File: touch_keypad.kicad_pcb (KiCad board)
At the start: 2 copper layers, 64.8 x 81.3 mm, 43 parts, among them J1 USB_B_Micro, J5 Conn_01x04_Female, SW1 SW_Push, SW10 SW_Push, SW11 SW_Push, SW12 SW_Push, SW13 SW_Push, SW14 SW_Push, SW15 SW_Push, SW16 SW_Push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

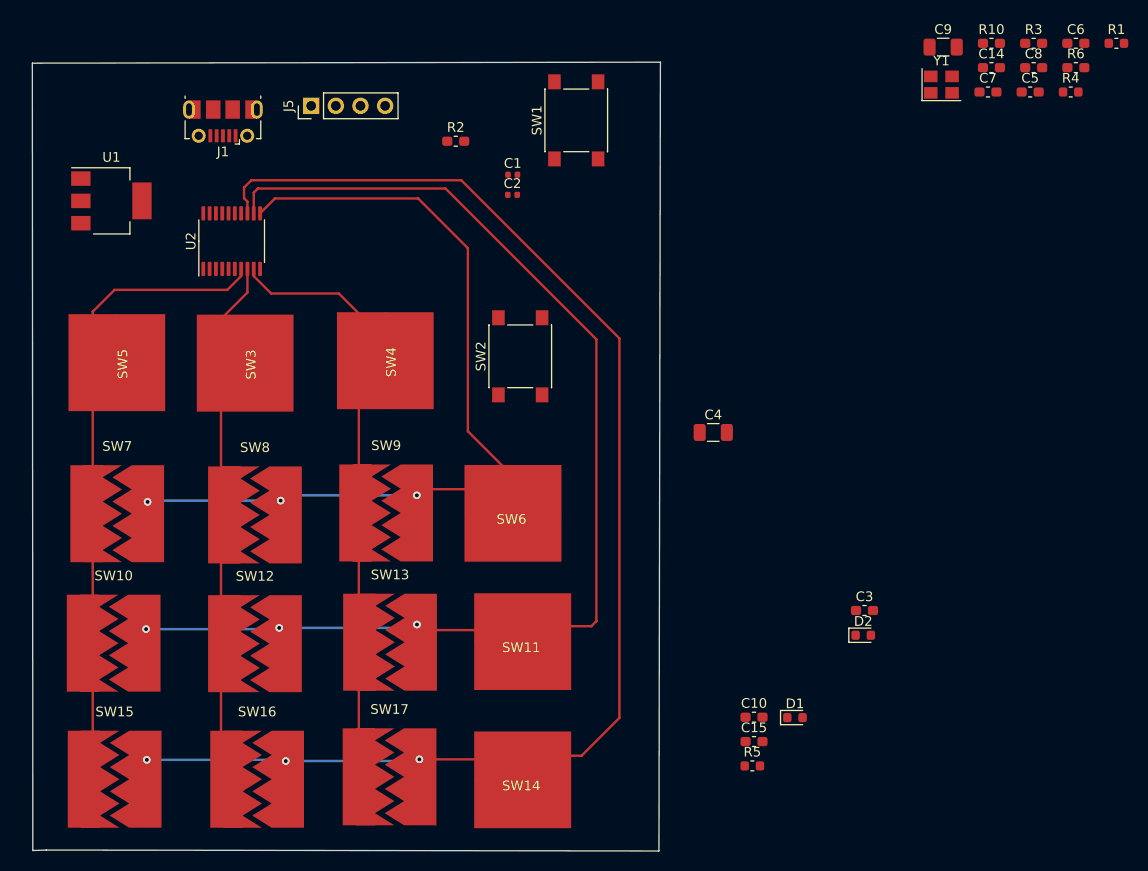
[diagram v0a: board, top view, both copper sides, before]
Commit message: upgrade to kicad 6
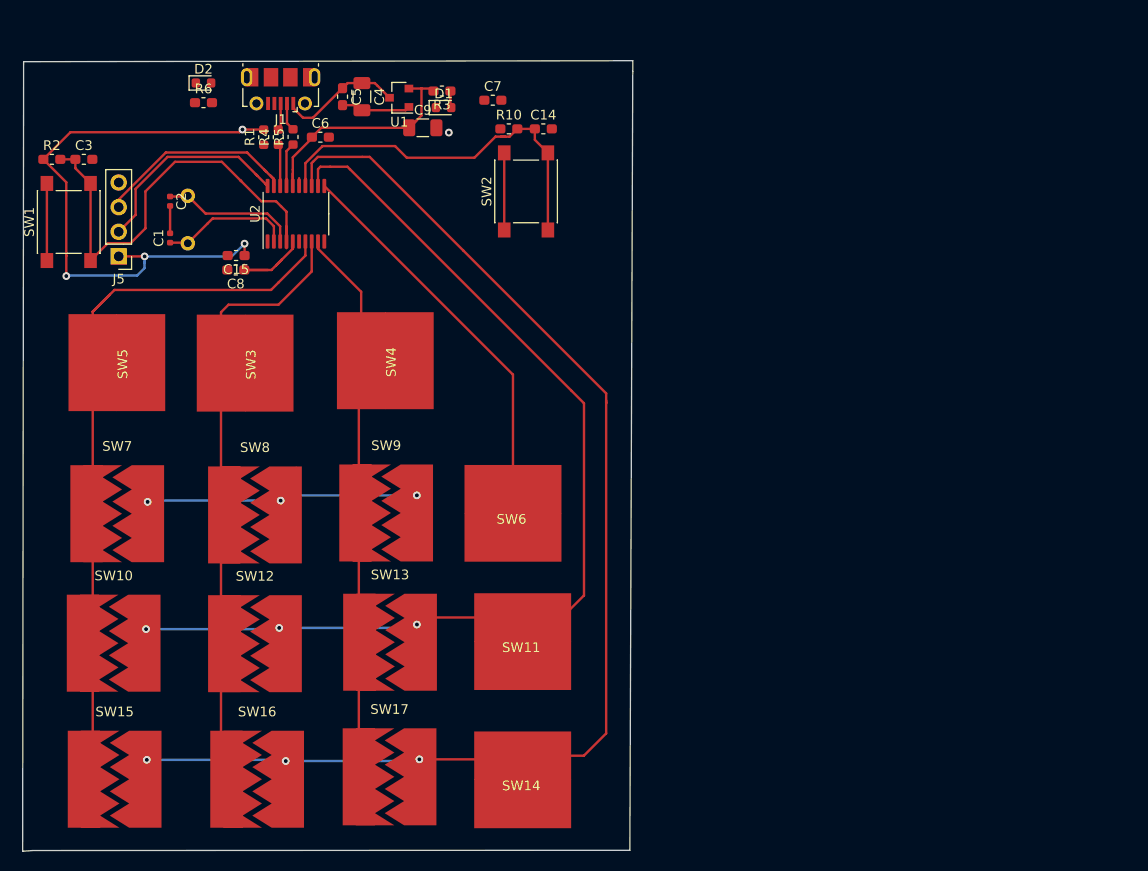
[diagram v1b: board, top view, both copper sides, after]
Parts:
- removed C10: 100n, Capacitor_SMD:C_0603_1608Metric_Pad1.05x0.95mm_HandSolder
- U1: value AMS1117-3.3 -> MCP1700-1802E_SOT23; footprint Package_TO_SOT_SMD:SOT-223-3_TabPin2 -> Package_TO_SOT_SMD:SOT-23
- Y1: value Crystal_GND24 -> Crystal; footprint Crystal:Crystal_SMD_3225-4Pin_3.2x2.5mm -> Crystal:Crystal_HC18-U_Vertical; moved to B.Cu
- moved C3 93.0 mm to (156.2, 61.5)
- moved R6 90.0 mm to (168.5, 55.6)
- moved D2 88.7 mm to (168.5, 53.6)
- moved R1 88.4 mm to (174.8, 59.2), turned to 90 degrees
- moved C8 84.9 mm to (171.9, 72.9), turned to 180 degrees
- moved R4 81.8 mm to (176.3, 59.2), turned to 90 degrees
- moved R5 80.3 mm to (177.8, 59.2), turned to 90 degrees
- moved Y1 79.4 mm to (166.9, 70.1), turned to 90 degrees
- moved C6 78.5 mm to (180.6, 59.2)
- moved C15 73.2 mm to (171.9, 71.4), turned to 180 degrees
- moved D1 72.6 mm to (193.3, 56.1)
- moved C5 70.9 mm to (182.9, 55.0), turned to -90 degrees
- moved R3 61.2 mm to (193.1, 54.4), turned to 180 degrees
- moved C9 54.3 mm to (191.2, 58.2)
- moved SW1 53.4 mm to (154.7, 67.9)
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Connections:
- C4 pad 1: Net-(C4-Pad1) -> +5V
- C5 pad 1: Net-(C4-Pad1) -> +5V
- C7 pad 1: +3V3 -> Net-(C7-Pad1)
- U1 pad 3: Net-(C4-Pad1) -> +5V
- U2 pad 2: Net-(U2-Pad2) -> Net-(C1-Pad1)
- U2 pad 3: Net-(U2-Pad3) -> Net-(C2-Pad1)
- Y1 pad 1: Net-(U2-Pad2) -> Net-(C1-Pad1)
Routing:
- net +3V3: track 0.00 -> 98.7 mm, vias 0 -> 5
- net NRST: track 0.00 -> 47.1 mm
- net Button7: track 0.00 -> 40.6 mm
- net Button2: track 60.2 -> 89.0 mm
- net GND: track 0.00 -> 27.0 mm
- net SWDIO: track 0.00 -> 22.7 mm
- net SWCLK: track 0.00 -> 22.0 mm
- net Button4: track 142.6 -> 121.5 mm
- net Net-(C2-Pad1): track 0.00 -> 14.3 mm
- net Net-(C1-Pad1): track 0.00 -> 13.7 mm
- net +5V: track 0.00 -> 12.9 mm
- net Button6: track 138.3 -> 150.2 mm
- net Button1: track 70.0 -> 81.1 mm
- net USB_D-: track 0.00 -> 5.29 mm
- net USB_D+: track 0.00 -> 5.06 mm
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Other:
- board size 64.8 x 81.3 mm -> 62.9 x 81.5 mm
- net class Default removed
